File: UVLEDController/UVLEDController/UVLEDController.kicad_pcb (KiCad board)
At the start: 2 copper layers, 100 x 36 mm, 15 parts, among them J1 Screw_Terminal_01x02, J2 Screw_Terminal_01x02, J3 Conn_01x04_Male, Q1 Q_NMOS_GDS

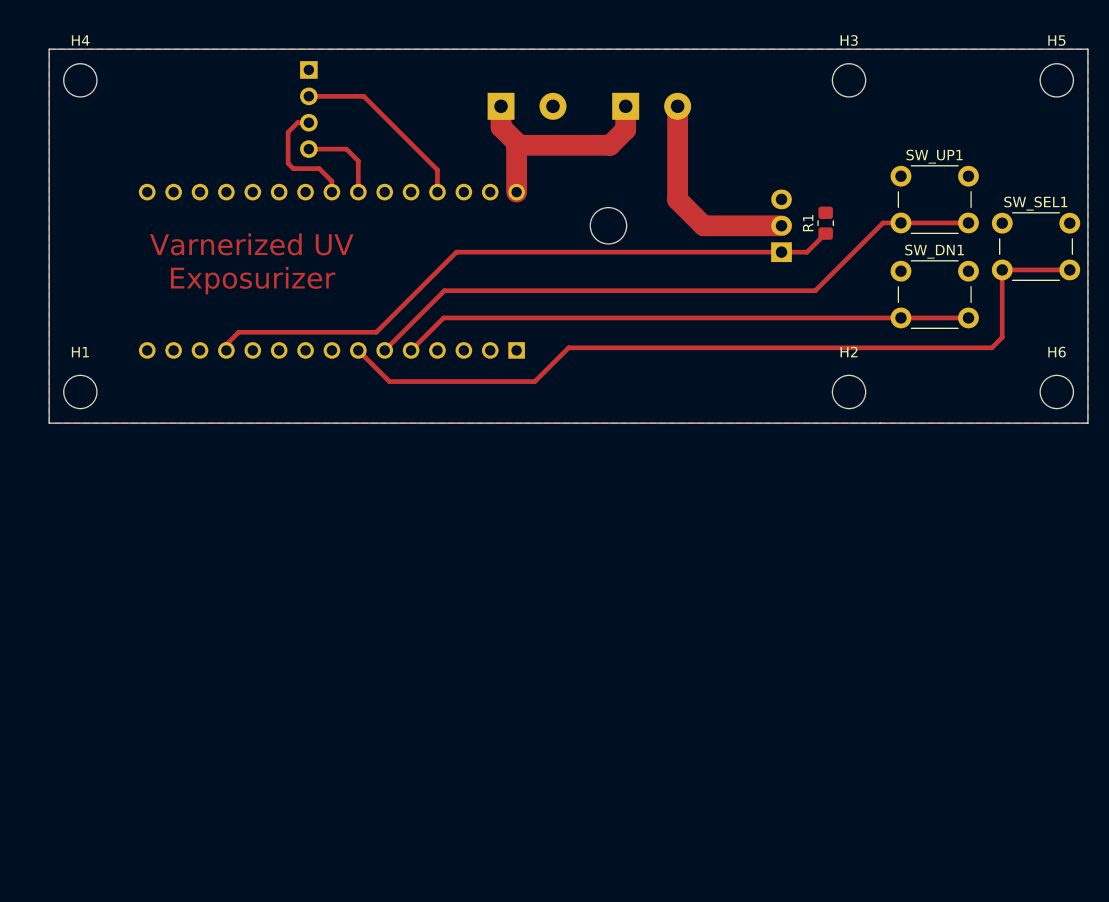
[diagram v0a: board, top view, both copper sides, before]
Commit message: Updates for physical dimensions based on Fuseion360 test fits.
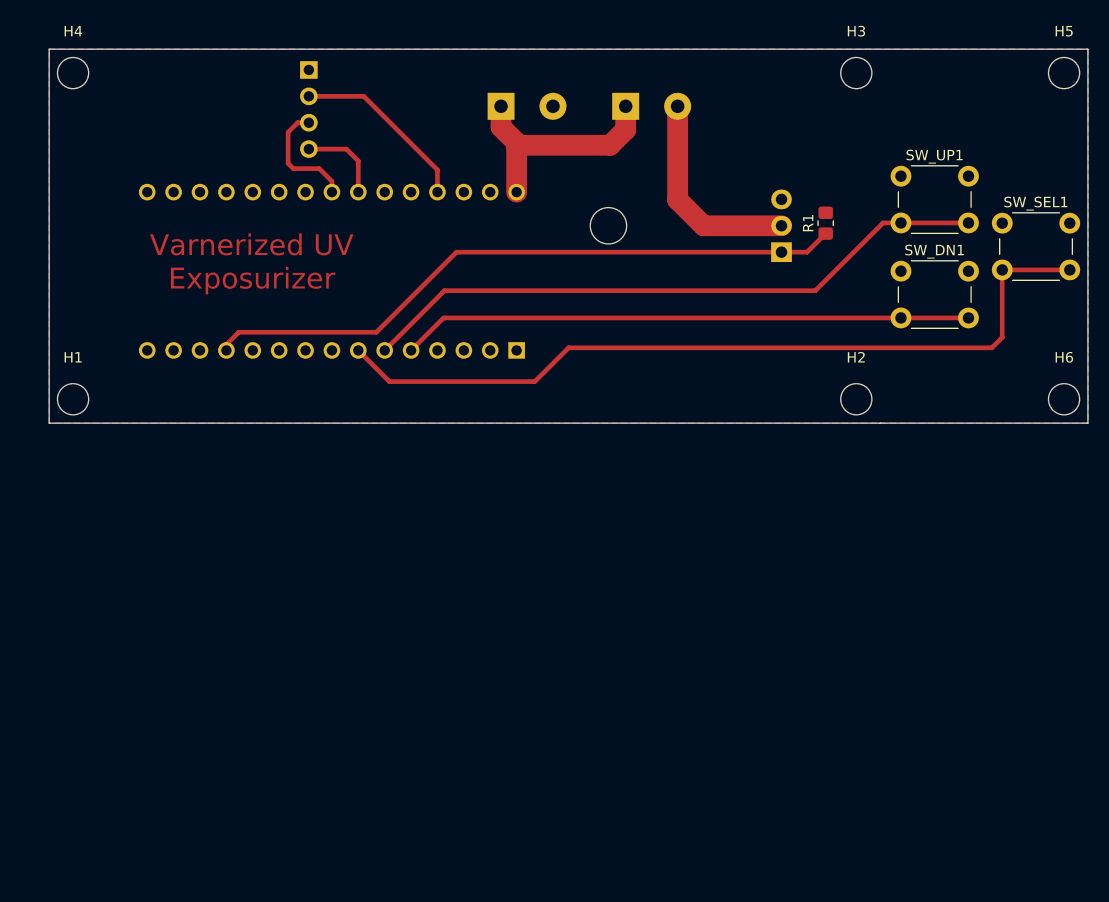
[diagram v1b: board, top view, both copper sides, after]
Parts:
- H1, H2, H3, H4, H5, H6: footprint MountingHole:MountingHole_3.2mm_M3_DIN965 -> MountingHole:MountingHole_3mm
- moved H1 0.99 mm to (122.3, 63.7)
- moved H4 0.99 mm to (122.3, 32.3)
- moved H2 0.99 mm to (197.7, 63.7)
- moved H3 0.99 mm to (197.7, 32.3)
- moved H5 0.99 mm to (217.7, 32.3)
- moved H6 0.99 mm to (217.7, 63.7)

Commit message: Moved the buttons to below the screen.
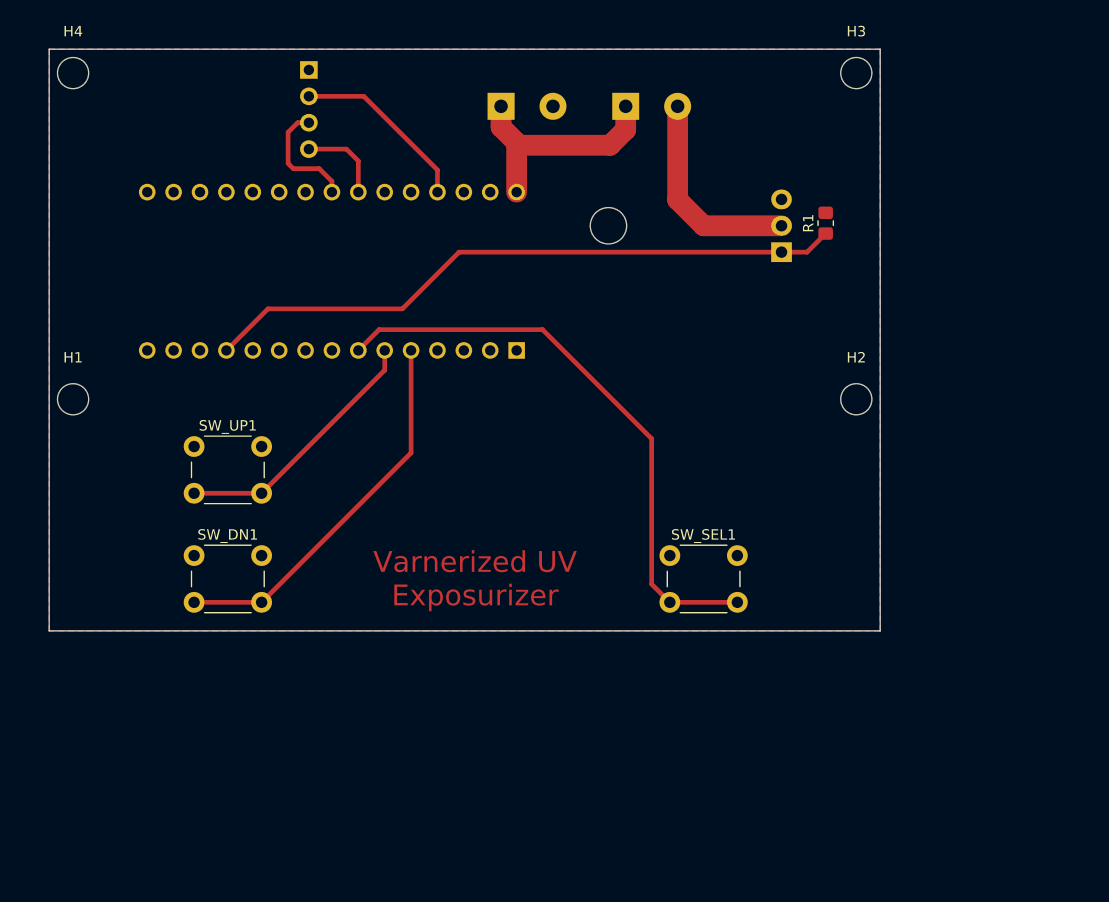
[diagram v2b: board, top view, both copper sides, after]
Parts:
- removed H5, H6: MountingHole, MountingHole:MountingHole_3mm
- moved SW_DN1 73.4 mm to (133.9, 78.8)
- moved SW_UP1 72.9 mm to (133.9, 68.2)
- moved SW_SEL1 45.3 mm to (179.8, 78.8)
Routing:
- net Net-(A1-Pad6): track 62.2 -> 25.2 mm
- net Net-(A1-Pad7): track 78.0 -> 56.4 mm
- net Net-(A1-Pad5): track 55.1 -> 36.7 mm
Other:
- board size 100 x 36 mm -> 80 x 56 mm
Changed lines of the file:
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@@
-  )
-  (footprint "MountingHole:MountingHole_3mm" (layer "F.Cu")
-    (at 217.7 63.7)
-    (descr "Mounting Hole 3mm, no annular")
-    (tags "mounting hole 3mm no annular")
-    (property "Sheetfile" "UVLEDController.kicad_sch")
-    (property "Sheetname" "")
-    (attr exclude_from_pos_files)
-    (fp_text reference "H6" (at 0 -4) (layer "F.SilkS")
-      (effects (font (size 1 1) (thickness 0.15)))
-    )
-    (fp_text value "MountingHole" (at 0 4) (layer "F.Fab")
-      (effects (font (size 1 1) (thickness 0.15)))
-    )
-    (fp_text user "${REFERENCE}" (at 0 0) (layer "F.Fab")
-      (effects (font (size 1 1) (thickness 0.15)))
-    )
-    (fp_circle (center 0 0) (end 3 0) (layer "Cmts.User") (width 0.15) (fill none))
-    (fp_circle (center 0 0) (end 3.25 0) (layer "F.CrtYd") (width 0.05) (fill none))
-    (pad "" np_thru_hole circle (at 0 0) (size 3 3) (drill 3) (layers *.Cu *.Mask))
   )
   (footprint "MountingHole:MountingHole_3mm" (layer "F.Cu")
@@
   )
   (footprint "Button_Switch_THT:SW_PUSH_6mm" (layer "F.Cu")
-    (at 202 51.372)
+    (at 133.95 78.75)
     (descr "https://www.omron.com/ecb/products/pdf/en-b3f.pdf")
     (tags "tact sw push 6mm")
@@
   )
   (footprint "Button_Switch_THT:SW_PUSH_6mm" (layer "F.Cu")
-    (at 211.75 46.75)
+    (at 179.75 78.75)
     (descr "https://www.omron.com/ecb/products/pdf/en-b3f.pdf")
     (tags "tact sw push 6mm")
@@
     )
   )
-  (footprint "MountingHole:MountingHole_3mm" (layer "F.Cu")
-    (at 217.7 32.3)
-    (descr "Mounting Hole 3mm, no annular")
-    (tags "mounting hole 3mm no annular")
-    (property "Sheetfile" "UVLEDController.kicad_sch")
-    (property "Sheetname" "")
-    (attr exclude_from_pos_files)
-    (fp_text reference "H5" (at 0 -4) (layer "F.SilkS")
-      (effects (font (size 1 1) (thickness 0.15)))
-    )
-    (fp_text value "MountingHole" (at 0 4) (layer "F.Fab")
-      (effects (font (size 1 1) (thickness 0.15)))
-    )
-    (fp_text user "${REFERENCE}" (at 0 0) (layer "F.Fab")
-      (effects (font (size 1 1) (thickness 0.15)))
-    )
-    (fp_circle (center 0 0) (end 3 0) (layer "Cmts.User") (width 0.15) (fill none))
-    (fp_circle (center 0 0) (end 3.25 0) (layer "F.CrtYd") (width 0.05) (fill none))
-    (pad "" np_thru_hole circle (at 0 0) (size 3 3) (drill 3) (layers *.Cu *.Mask))
-  )
   (footprint "Button_Switch_THT:SW_PUSH_6mm" (layer "F.Cu")
-    (at 202 42.228)
+    (at 133.95 68.25)
     (descr "https://www.omron.com/ecb/products/pdf/en-b3f.pdf")
     (tags "tact sw push 6mm")
@@
     )
   )
-  (gr_line locked (start 120 66) (end 120 30) (layer "Edge.Cuts") (width 0.1))
-  (gr_line (start 220 66) (end 200 66) (layer "Edge.Cuts") (width 0.1))
-  (gr_line (start 220 30) (end 220 66) (layer "Edge.Cuts") (width 0.1))
-  (gr_line (start 200 66) (end 120 66) (layer "Edge.Cuts") (width 0.1))
-  (gr_line (start 220 30) (end 120 30) (layer "Edge.Cuts") (width 0.1))
-  (gr_line (start 223 66) (end 223 56) (layer "User.1") (width 0.15))
-  (gr_line (start 223 42) (end 223 30) (layer "User.1") (width 0.15))
-  (gr_line (start 225 42) (end 223 42) (layer "User.1") (width 0.15))
-  (gr_line (start 225 56) (end 225 42) (layer "User.1") (width 0.15))
-  (gr_line (start 223 56) (end 225 56) (layer "User.1") (width 0.15))
-  (gr_text "Varnerized UV\nExposurizer" (at 139.5 50.5) (layer "F.Cu")
+  (gr_line (start 120 86) (end 120 30) (layer "Edge.Cuts") (width 0.1))
+  (gr_line (start 200 86) (end 120 86) (layer "Edge.Cuts") (width 0.1))
+  (gr_line (start 200 86) (end 200 30) (layer "Edge.Cuts") (width 0.1))
+  (gr_line (start 200 30) (end 120 30) (layer "Edge.Cuts") (width 0.1))
+  (gr_text "Varnerized UV\nExposurizer" (at 161 81) (layer "F.Cu")
     (effects (font (size 2 2) (thickness 0.3)))
   )
   (dimension (type aligned) (layer "User.1")
-    (pts (xy 200 30) (xy 220 30))
-    (height -7)
-    (gr_text "20.0000 mm" (at 210 21.85) (layer "User.1")
-      (effects (font (size 1 1) (thickness 0.15)))
-    )
-    (format (units 3) (units_format 1) (precision 4))
-    (style (thickness 0.15) (arrow_length 1.27) (text_position_mode 0) (extension_height 0.58642) (extension_offset 0.5) keep_text_aligned)
-  )
-  (dimension (type aligned) (layer "User.1")
-    (pts (xy 120 30) (xy 120 66))
+    (pts (xy 120 30) (xy 120 86))
     (height 4)
-    (gr_text "36.0000 mm" (at 114.85 48 90) (layer "User.1")
+    (gr_text "56.0000 mm" (at 114.85 58 90) (layer "User.1")
       (effects (font (size 1 1) (thickness 0.15)))
     )
@@
     (style (thickness 0.15) (arrow_length 1.27) (text_position_mode 0) (extension_height 0.58642) (extension_offset 0.5) keep_text_aligned)
   )
-  (segment (start 202.142 55.872) (end 157.968 55.872) (width 0.45) (layer "F.Cu") (net 5))
-  (segment (start 208.642 55.872) (end 202.142 55.872) (width 0.45) (layer "F.Cu") (net 5))
-  (segment (start 157.968 55.872) (end 154.84 59) (width 0.45) (layer "F.Cu") (net 5))
-  (segment (start 208.582 46.728) (end 201.272 46.728) (width 0.45) (layer "F.Cu") (net 6))
-  (segment (start 200.272 46.728) (end 193.75 53.25) (width 0.45) (layer "F.Cu") (net 6))
-  (segment (start 202.082 46.728) (end 200.272 46.728) (width 0.45) (layer "F.Cu") (net 6))
-  (segment (start 158.05 53.25) (end 152.3 59) (width 0.45) (layer "F.Cu") (net 6))
-  (segment (start 193.75 53.25) (end 158.05 53.25) (width 0.45) (layer "F.Cu") (net 6))
-  (segment (start 170.002 58.748) (end 210.748 58.748) (width 0.45) (layer "F.Cu") (net 7))
-  (segment (start 149.76 59) (end 152.76 62) (width 0.45) (layer "F.Cu") (net 7))
-  (segment (start 152.76 62) (end 166.75 62) (width 0.45) (layer "F.Cu") (net 7))
-  (segment (start 211.746 57.75) (end 211.746 51.25) (width 0.45) (layer "F.Cu") (net 7))
-  (segment (start 166.75 62) (end 170.002 58.748) (width 0.45) (layer "F.Cu") (net 7))
-  (segment (start 211.746 51.25) (end 218.246 51.25) (width 0.45) (layer "F.Cu") (net 7))
-  (segment (start 210.748 58.748) (end 211.746 57.75) (width 0.45) (layer "F.Cu") (net 7))
+  (segment (start 154.84 68.86) (end 140.45 83.25) (width 0.45) (layer "F.Cu") (net 5))
+  (segment (start 133.95 83.25) (end 140.45 83.25) (width 0.45) (layer "F.Cu") (net 5))
+  (segment (start 154.84 59) (end 154.84 68.86) (width 0.45) (layer "F.Cu") (net 5))
+  (segment (start 133.95 72.75) (end 140.45 72.75) (width 0.45) (layer "F.Cu") (net 6))
+  (segment (start 152.3 59) (end 152.3 60.9) (width 0.45) (layer "F.Cu") (net 6))
+  (segment (start 152.3 60.9) (end 140.45 72.75) (width 0.45) (layer "F.Cu") (net 6))
+  (segment (start 179.75 83.25) (end 186.25 83.25) (width 0.45) (layer "F.Cu") (net 7))
+  (segment (start 151.76 57) (end 167.5 57) (width 0.45) (layer "F.Cu") (net 7))
+  (segment (start 167.5 57) (end 178 67.5) (width 0.45) (layer "F.Cu") (net 7))
+  (segment (start 178 67.5) (end 178 81.5) (width 0.45) (layer "F.Cu") (net 7))
+  (segment (start 149.76 59) (end 151.76 57) (width 0.45) (layer "F.Cu") (net 7))
+  (segment (start 178 81.5) (end 179.75 83.25) (width 0.45) (layer "F.Cu") (net 7))
   (segment (start 194.75 47.75) (end 192.96 49.54) (width 0.45) (layer "F.Cu") (net 12))
-  (segment (start 151.5 57.25) (end 138.25 57.25) (width 0.45) (layer "F.Cu") (net 12))
-  (segment (start 159.21 49.54) (end 151.5 57.25) (width 0.45) (layer "F.Cu") (net 12))
   (segment (start 192.96 49.54) (end 190.5 49.54) (width 0.45) (layer "F.Cu") (net 12))
-  (segment (start 138.25 57.25) (end 137.06 58.44) (width 0.45) (layer "F.Cu") (net 12))
+  (segment (start 154 55) (end 141.06 55) (width 0.45) (layer "F.Cu") (net 12))
   (segment (start 137.06 58.44) (end 137.06 59) (width 0.45) (layer "F.Cu") (net 12))
-  (segment (start 190.5 49.54) (end 159.21 49.54) (width 0.45) (layer "F.Cu") (net 12))
+  (segment (start 159.46 49.54) (end 154 55) (width 0.45) (layer "F.Cu") (net 12))
+  (segment (start 141.06 55) (end 137.06 59) (width 0.45) (layer "F.Cu") (net 12))
+  (segment (start 190.5 49.54) (end 159.46 49.54) (width 0.45) (layer "F.Cu") (net 12))
   (segment (start 147.22 42.72) (end 146 41.5) (width 0.45) (layer "F.Cu") (net 23))
   (segment (start 143.5 41.5) (end 143 41) (width 0.45) (layer "F.Cu") (net 23))
@@
     (polygon
       (pts
-        (xy 220 66)
-        (xy 120 66)
+        (xy 200 86)
+        (xy 120 86)
         (xy 120 30)
-        (xy 220 30)
+        (xy 200 30)
       )
     )

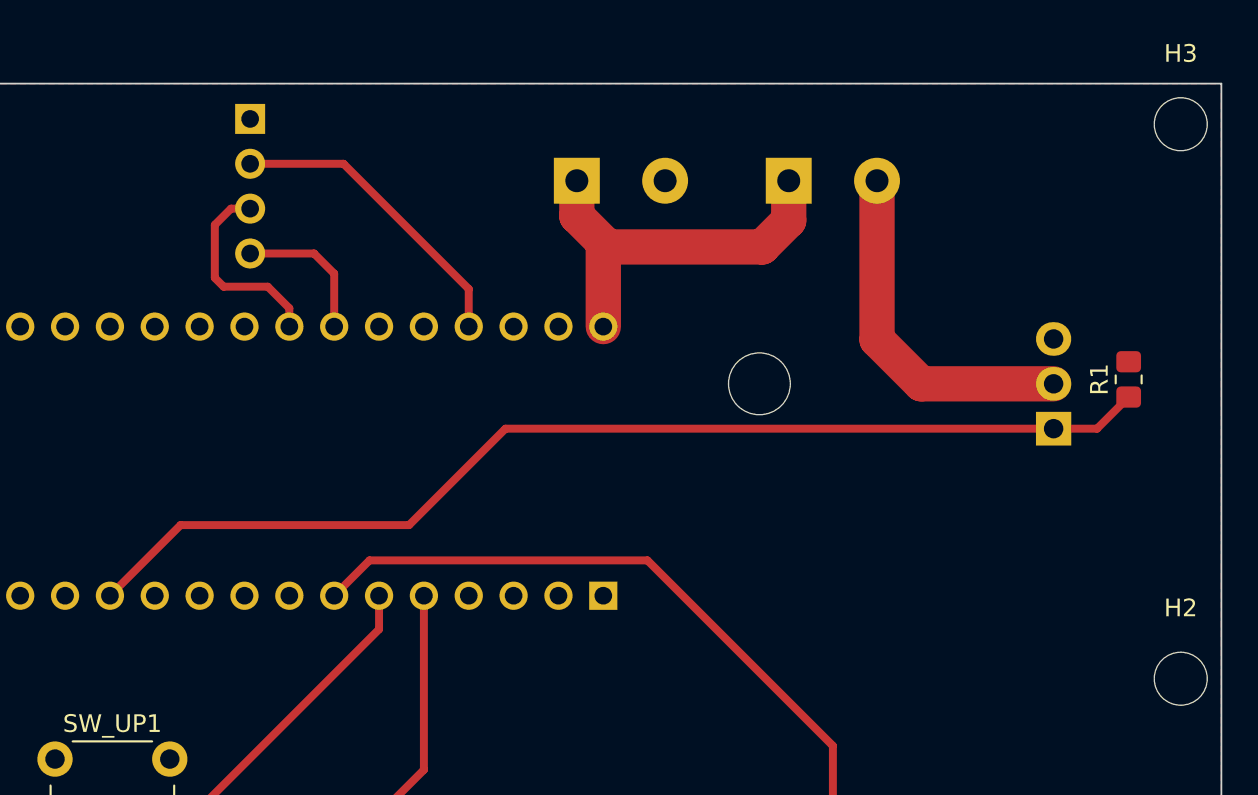
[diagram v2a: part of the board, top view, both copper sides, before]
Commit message: Moved the screw terminals to a better location. Tweaked position of i2c header.
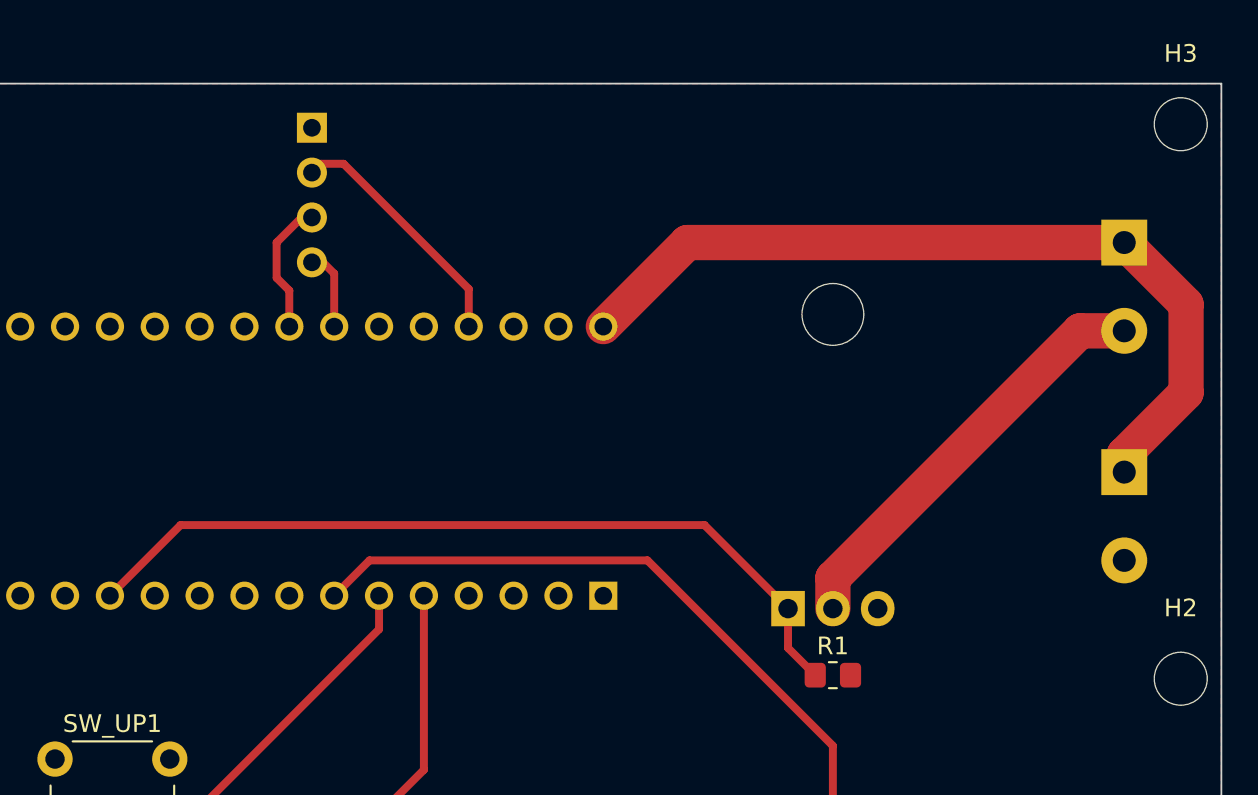
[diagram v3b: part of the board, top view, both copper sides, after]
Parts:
- moved J2-PWR1 35.1 mm to (194.5, 52.0), turned to -90 degrees
- moved R1 23.7 mm to (178.0, 63.5), turned to 0 degrees
- moved J1-LED1 19.3 mm to (194.5, 39.0), turned to -90 degrees
- moved Q1 18.2 mm to (175.5, 59.7), turned to 0 degrees
- moved J3 3.54 mm to (148.5, 32.5)
- renumbered J1 to J1-LED1, J2 to J2-PWR1
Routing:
- net Net-(A1-Pad30): track 22.4 -> 47.4 mm
- net Net-(A1-Pad12): track 62.9 -> 46.4 mm
- net Net-(J1-LED1-Pad2): track 20.0 -> 24.0 mm
- net Net-(A1-Pad24): track 8.23 -> 4.53 mm
- net Net-(A1-Pad23): track 11.4 -> 7.65 mm
- net Net-(A1-Pad27): track 17.4 -> 14.2 mm

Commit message: Rotated.
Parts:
- moved H4 75.4 mm to (122.3, 107.7), turned to 90 degrees
- moved H3 75.4 mm to (122.3, 32.3), turned to 90 degrees
- moved J1-LED1 65.6 mm to (129.0, 35.5), turned to 0 degrees
- moved J3 55.5 mm to (122.5, 81.5), turned to -90 degrees
- moved J2-PWR1 55.0 mm to (142.0, 35.5), turned to 0 degrees
- moved H1 54.1 mm to (153.7, 107.7), turned to 90 degrees
- moved H2 54.1 mm to (153.7, 32.3), turned to 90 degrees
- moved SW_DN1 38.9 mm to (168.8, 96.0), turned to 90 degrees
- moved SW_UP1 36.9 mm to (158.2, 96.0), turned to 90 degrees
- moved SW_SEL1 30.5 mm to (168.8, 50.2), turned to 90 degrees
- moved R1 27.1 mm to (153.5, 52.0), turned to 90 degrees
- moved Q1 26.2 mm to (149.7, 54.5), turned to 90 degrees
- moved A1 17.1 mm to (149.0, 65.0), turned to 180 degrees
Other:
- board size 80 x 56 mm -> 56 x 80 mm
